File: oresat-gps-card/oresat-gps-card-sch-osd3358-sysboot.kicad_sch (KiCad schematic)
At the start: 23 parts, among them J2 Conn_01x02, J5 Conn_01x06, U1 OSD3358-512M-BSM

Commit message: Routine Push
Various small changes made
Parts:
- removed TP114, TP115, TP116, TP117, TP118, TP119, TP120, TP121, TP122, TP123, TP124, TP125, TP126: 0.03x0.04, oresat-misc:TestPoint_Pad_D1.0mm, symbol oresat-misc:Test-Point-1mm-round

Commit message: Routine Push
First attempt to clean up schematic
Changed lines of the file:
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@@
 		)
 	)
-	(global_label "GPS-EN"
+	(hierarchical_label "MAX_~{SHDN}"
 		(shape input)
-		(at 33.02 124.46 180)
-		(fields_autoplaced yes)
+		(at 33.02 99.06 180)
 		(effects
 			(font
@@
 			(justify right)
 		)
-		(property "Intersheetrefs" "${INTERSHEET_REFS}"
-			(at 22.8055 124.3806 0)
-			(show_name no)
-			(do_not_autoplace no)
-			(effects
-				(font
-					(size 1.27 1.27)
-				)
-				(justify right)
-			)
-		)
 	)
-	(global_label "STQ_UART2_TX"
+	(hierarchical_label "MAX_SPI1_CS0"
 		(shape input)
-		(at 53.34 165.1 270)
-		(fields_autoplaced yes)
+		(at 48.26 165.1 270)
 		(effects
 			(font
@@
 			(justify right)
 		)
-		(property "Intersheetrefs" "${INTERSHEET_REFS}"
-			(at 53.2606 180.9993 90)
-			(show_name no)
-			(do_not_autoplace no)
-			(effects
-				(font
-					(size 1.27 1.27)
-				)
-				(justify right)
+	)
+	(hierarchical_label "GPS-EN"
+		(shape input)
+		(at 33.02 124.46 180)
+		(effects
+			(font
+				(size 1.27 1.27)
 			)
+			(justify right)
 		)
 	)
-	(global_label "SYSBOOT2"
+	(hierarchical_label "MAX_SPI1_D0"
+		(shape input)
+		(at 43.18 165.1 270)
+		(effects
+			(font
+				(size 1.27 1.27)
+			)
+			(justify right)
+		)
+	)
+	(hierarchical_label "STQ_UART2_TX"
+		(shape input)
+		(at 53.34 165.1 270)
+		(effects
+			(font
+				(size 1.27 1.27)
+			)
+			(justify right)
+		)
+	)
+	(hierarchical_label "STQ_UART2_RX"
+		(shape input)
+		(at 50.8 165.1 270)
+		(effects
+			(font
+				(size 1.27 1.27)
+			)
+			(justify right)
+		)
+	)
+	(hierarchical_label "SYSBOOT2"
 		(shape input)
 		(at 220.98 109.22 0)
-		(fields_autoplaced yes)
 		(effects
 			(font
@@
 			(justify left)
 		)
-		(property "Intersheetrefs" "${INTERSHEET_REFS}"
-			(at 233.5015 109.22 0)
-			(show_name no)
-			(do_not_autoplace no)
-			(effects
-				(font
-					(size 1.27 1.27)
-				)
-				(justify left)
-			)
-		)
 	)
-	(global_label "STQ_UART2_RX"
+	(hierarchical_label "MAX_SPI1_SCLK"
 		(shape input)
-		(at 50.8 165.1 270)
-		(fields_autoplaced yes)
+		(at 45.72 165.1 270)
 		(effects
 			(font
@@
 			(justify right)
 		)
-		(property "Intersheetrefs" "${INTERSHEET_REFS}"
-			(at 50.7206 181.3017 90)
-			(show_name no)
-			(do_not_autoplace no)
-			(effects
-				(font
-					(size 1.27 1.27)
-				)
-				(justify right)
-			)
-		)
 	)
-	(global_label "STQ-1PPS"
+	(hierarchical_label "STQ-1PPS"
 		(shape input)
 		(at 33.02 121.92 180)
-		(fields_autoplaced yes)
 		(effects
 			(font
@@
 			(justify right)
 		)
-		(property "Intersheetrefs" "${INTERSHEET_REFS}"
-			(at 20.5679 121.8406 0)
-			(show_name no)
-			(do_not_autoplace no)
-			(effects
-				(font
-					(size 1.27 1.27)
-				)
-				(justify right)
-			)
-		)
 	)
-	(global_label "MAX_SPI1_CS0"
+	(hierarchical_label "MAX-LD"
 		(shape input)
-		(at 48.26 165.1 270)
-		(fields_autoplaced yes)
+		(at 33.02 96.52 180)
 		(effects
 			(font
@@
 			(justify right)
 		)
-		(property "Intersheetrefs" "${INTERSHEET_REFS}"
-			(at 48.1806 181.1807 90)
-			(show_name no)
-			(do_not_autoplace no)
-			(effects
-				(font
-					(size 1.27 1.27)
-				)
-				(justify right)
-			)
-		)
 	)
-	(global_label "MAX_SPI1_D0"
-		(shape input)
-		(at 43.18 165.1 270)
-		(fields_autoplaced yes)
-		(effects
-			(font
-				(size 1.27 1.27)
-			)
-			(justify right)
-		)
-		(property "Intersheetrefs" "${INTERSHEET_REFS}"
-			(at 43.1006 179.9712 90)
-			(show_name no)
-			(do_not_autoplace no)
-			(effects
-				(font
-					(size 1.27 1.27)
-				)
-				(justify right)
-			)
-		)
-	)
-	(global_label "MAX_~{SHDN}"
-		(shape input)
-		(at 33.02 99.06 180)
-		(fields_autoplaced yes)
-		(effects
-			(font
-				(size 1.27 1.27)
-			)
-			(justify right)
-		)
-		(property "Intersheetrefs" "${INTERSHEET_REFS}"
-			(at 20.7493 98.9806 0)
-			(show_name no)
-			(do_not_autoplace no)
-			(effects
-				(font
-					(size 1.27 1.27)
-				)
-				(justify right)
-			)
-		)
-	)
-	(global_label "MAX-LD"
-		(shape input)
-		(at 33.02 96.52 180)
-		(fields_autoplaced yes)
-		(effects
-			(font
-				(size 1.27 1.27)
-			)
-			(justify right)
-		)
-		(property "Intersheetrefs" "${INTERSHEET_REFS}"
-			(at 23.5917 96.4406 0)
-			(show_name no)
-			(do_not_autoplace no)
-			(effects
-				(font
-					(size 1.27 1.27)
-				)
-				(justify right)
-			)
-		)
-	)
-	(global_label "MAX_SPI1_SCLK"
-		(shape input)
-		(at 45.72 165.1 270)
-		(fields_autoplaced yes)
-		(effects
-			(font
-				(size 1.27 1.27)
-			)
-			(justify right)
-		)
-		(property "Intersheetrefs" "${INTERSHEET_REFS}"
-			(at 45.6406 182.2693 90)
-			(show_name no)
-			(do_not_autoplace no)
-			(effects
-				(font
-					(size 1.27 1.27)
-				)
-				(justify right)
-			)
-		)
-	)

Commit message: Routine Push
Schematic finished. Components laid out, chasing ERCs.
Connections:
- no-connect marks 8 -> 21
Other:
- moved on the sheet: J2, J5, R72, R73, R74, TP111, TP112, TP113, TP20, U1D

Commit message: Routine Push
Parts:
- removed TP111, TP112, TP113, TP20: 0.03x0.04, oresat-misc:TestPoint_Pad_D1.0mm, symbol oresat-misc:Test-Point-1mm-round
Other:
- note added: "All resistors are 0603 1% AEC-Q200 unless marked. All capacitors are 0603 AEC-Q200 Vw >= 16V X5R or better unless marked."

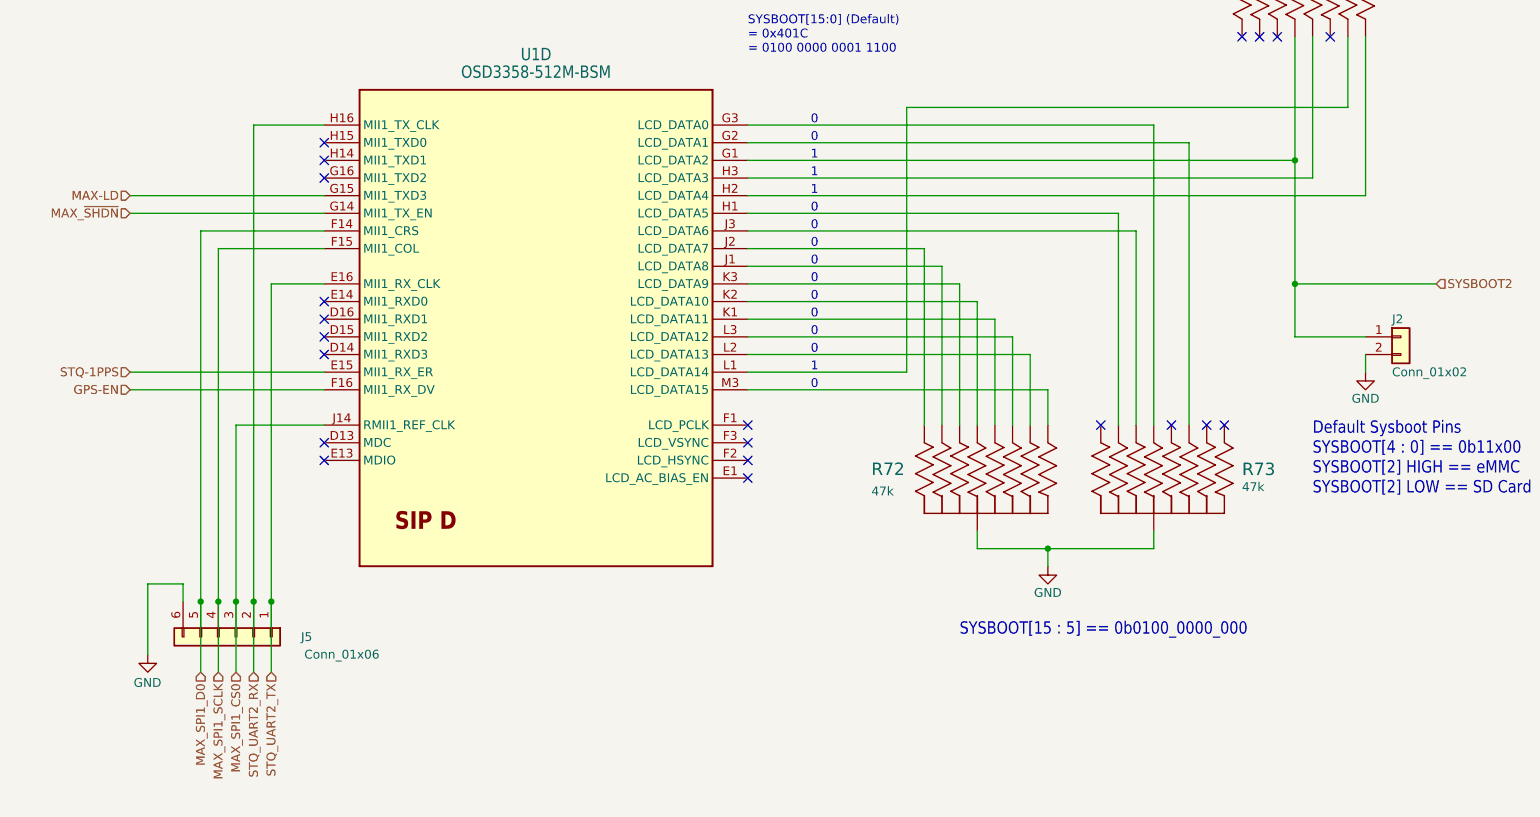
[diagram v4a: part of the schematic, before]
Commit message: General cleanup of schematic and layout
Updated .gitignore, updates DRU file, moved RF lines to RF-50-MIN (max is just too big),
lots of cleanup on the root page to make it pretty, cleaned up some redudant labels,
updated SMPM connector and added rule zone, updated PCB outline to include NPTH drills
for SMPM connectors, began cleanup of OPD.
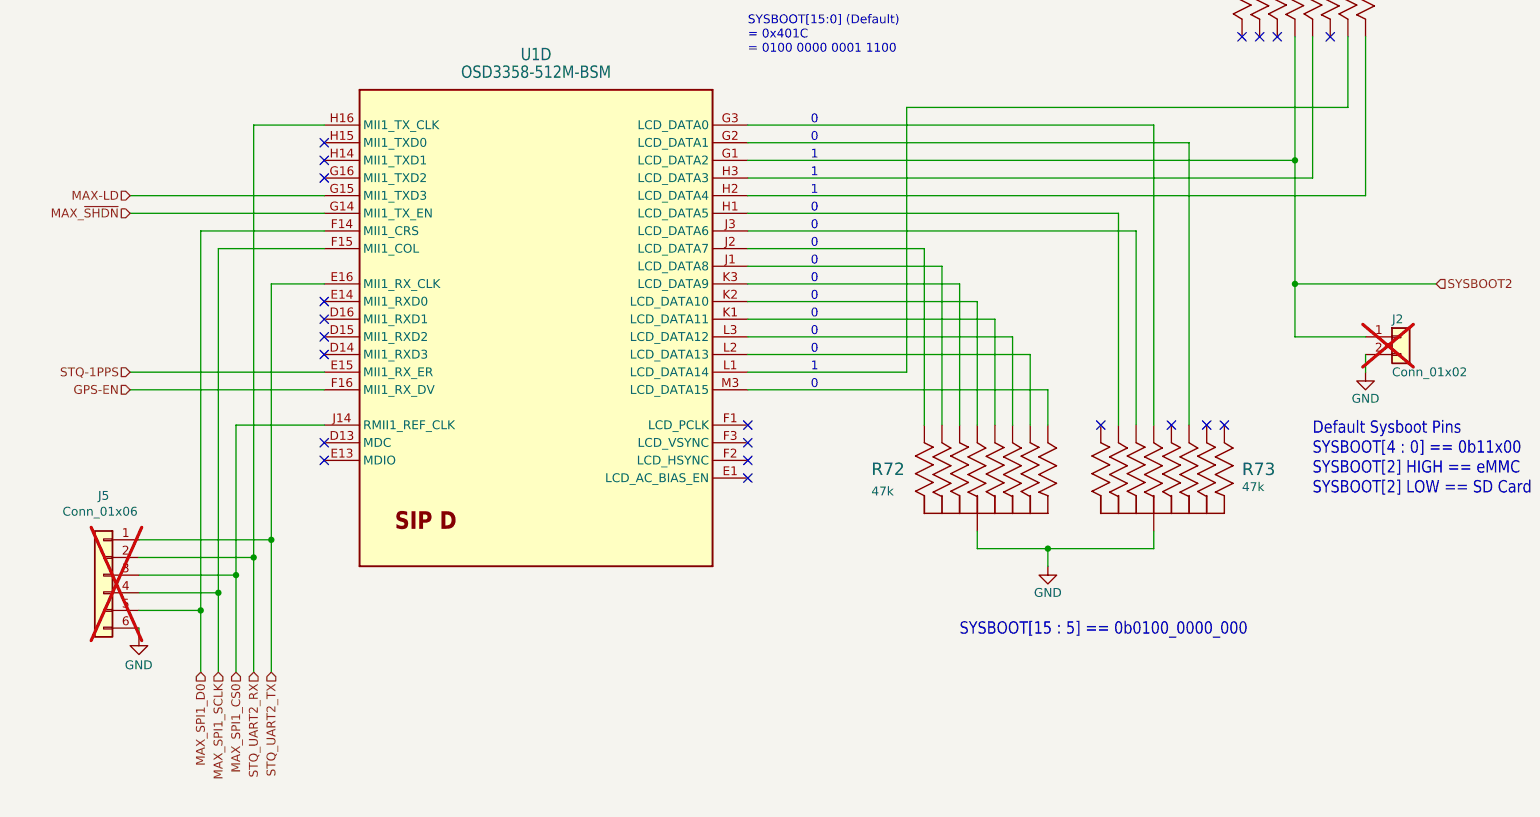
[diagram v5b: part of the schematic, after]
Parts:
- J2, J5: now not fitted
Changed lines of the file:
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@@
 	)
 	(junction
-		(at 138.43 184.15)
+		(at 140.97 180.34)
 		(diameter 0)
 		(color 0 0 0 0)
 	)
 	(junction
-		(at 146.05 184.15)
+		(at 135.89 185.42)
 		(diameter 0)
 		(color 0 0 0 0)
 	)
 	(junction
-		(at 143.51 184.15)
+		(at 143.51 177.8)
 		(diameter 0)
 		(color 0 0 0 0)
 	)
 	(junction
-		(at 135.89 184.15)
-		(diameter 0)
-		(color 0 0 0 0)
-	)
-	(junction
-		(at 140.97 184.15)
+		(at 146.05 175.26)
 		(diameter 0)
 		(color 0 0 0 0)
@@
 		(color 0 0 0 0)
 	)
+	(junction
+		(at 138.43 182.88)
+		(diameter 0)
+		(color 0 0 0 0)
+	)
 	(no_connect
 		(at 153.67 148.59)
@@
 	(wire
 		(pts
-			(xy 133.35 184.15) (xy 133.35 181.61)
+			(xy 127 187.96) (xy 127 189.23)
 		)
 		(stroke
@@
 	(wire
 		(pts
+			(xy 127 182.88) (xy 138.43 182.88)
+		)
+		(stroke
+			(width 0)
+			(type default)
+		)
+	)
+	(wire
+		(pts
 			(xy 214.63 153.67) (xy 257.81 153.67)
 		)
@@
 	(wire
 		(pts
-			(xy 135.89 184.15) (xy 135.89 130.81)
+			(xy 135.89 130.81) (xy 135.89 185.42)
 		)
 		(stroke
@@
 	(wire
 		(pts
+			(xy 127 177.8) (xy 143.51 177.8)
+		)
+		(stroke
+			(width 0)
+			(type default)
+		)
+	)
+	(wire
+		(pts
 			(xy 214.63 135.89) (xy 242.57 135.89)
 		)
@@
 	(wire
 		(pts
+			(xy 140.97 180.34) (xy 140.97 194.31)
+		)
+		(stroke
+			(width 0)
+			(type default)
+		)
+	)
+	(wire
+		(pts
 			(xy 135.89 130.81) (xy 153.67 130.81)
 		)
@@
 	(wire
 		(pts
+			(xy 138.43 182.88) (xy 138.43 194.31)
+		)
+		(stroke
+			(width 0)
+			(type default)
+		)
+	)
+	(wire
+		(pts
 			(xy 214.63 115.57) (xy 273.05 115.57)
 		)
@@
 	(wire
 		(pts
-			(xy 133.35 181.61) (xy 128.27 181.61)
-		)
-		(stroke
-			(width 0)
-			(type default)
-		)
-	)
-	(wire
-		(pts
-			(xy 138.43 184.15) (xy 138.43 194.31)
+			(xy 143.51 177.8) (xy 143.51 194.31)
 		)
 		(stroke
@@
 	(wire
 		(pts
-			(xy 138.43 133.35) (xy 138.43 184.15)
-		)
-		(stroke
-			(width 0)
-			(type default)
-		)
-	)
-	(wire
-		(pts
 			(xy 247.65 176.53) (xy 257.81 176.53)
 		)
@@
 	(wire
 		(pts
-			(xy 146.05 138.43) (xy 146.05 184.15)
+			(xy 127 180.34) (xy 140.97 180.34)
 		)
 		(stroke
@@
 	(wire
 		(pts
+			(xy 127 185.42) (xy 135.89 185.42)
+		)
+		(stroke
+			(width 0)
+			(type default)
+		)
+	)
+	(wire
+		(pts
 			(xy 245.11 138.43) (xy 245.11 158.75)
 		)
@@
 	(wire
 		(pts
+			(xy 127 175.26) (xy 146.05 175.26)
+		)
+		(stroke
+			(width 0)
+			(type default)
+		)
+	)
+	(wire
+		(pts
 			(xy 240.03 133.35) (xy 240.03 158.75)
 		)
@@
 	(wire
 		(pts
-			(xy 128.27 181.61) (xy 128.27 191.77)
-		)
-		(stroke
-			(width 0)
-			(type default)
-		)
-	)
-	(wire
-		(pts
 			(xy 293.37 138.43) (xy 293.37 146.05)
 		)
@@
 	(wire
 		(pts
-			(xy 135.89 184.15) (xy 135.89 194.31)
+			(xy 135.89 185.42) (xy 135.89 194.31)
+		)
+		(stroke
+			(width 0)
+			(type default)
+		)
+	)
+	(wire
+		(pts
+			(xy 140.97 158.75) (xy 140.97 180.34)
 		)
 		(stroke
@@
 		)
 	)
-	(wire
-		(pts
-			(xy 143.51 115.57) (xy 143.51 184.15)
-		)
-		(stroke
-			(width 0)
-			(type default)
-		)
-	)
 	(polyline
 		(pts
@@
 	(wire
 		(pts
+			(xy 146.05 175.26) (xy 146.05 194.31)
+		)
+		(stroke
+			(width 0)
+			(type default)
+		)
+	)
+	(wire
+		(pts
 			(xy 214.63 148.59) (xy 255.27 148.59)
 		)
@@
 	(wire
 		(pts
-			(xy 140.97 184.15) (xy 140.97 158.75)
-		)
-		(stroke
-			(width 0)
-			(type default)
-		)
-	)
-	(wire
-		(pts
 			(xy 125.73 128.27) (xy 153.67 128.27)
 		)
@@
 	(wire
 		(pts
-			(xy 140.97 184.15) (xy 140.97 194.31)
-		)
-		(stroke
-			(width 0)
-			(type default)
-		)
-	)
-	(wire
-		(pts
 			(xy 214.63 138.43) (xy 245.11 138.43)
 		)
@@
 	(wire
 		(pts
+			(xy 143.51 115.57) (xy 143.51 177.8)
+		)
+		(stroke
+			(width 0)
+			(type default)
+		)
+	)
+	(wire
+		(pts
 			(xy 293.37 138.43) (xy 313.69 138.43)
 		)
@@
 	(wire
 		(pts
-			(xy 143.51 184.15) (xy 143.51 194.31)
-		)
-		(stroke
-			(width 0)
-			(type default)
-		)
-	)
-	(wire
-		(pts
-			(xy 146.05 184.15) (xy 146.05 194.31)
+			(xy 146.05 138.43) (xy 146.05 175.26)
 		)
 		(stroke
@@
 		(pts
 			(xy 295.91 85.09) (xy 295.91 87.63)
+		)
+		(stroke
+			(width 0)
+			(type default)
+		)
+	)
+	(wire
+		(pts
+			(xy 138.43 133.35) (xy 138.43 182.88)
 		)
 		(stroke
@@
 		(on_board yes)
 		(in_pos_files yes)
-		(dnp no)
+		(dnp yes)
 		(property "Reference" "J2"
 			(at 307.34 143.51 0)
@@
 	(symbol
 		(lib_id "Connector_Generic:Conn_01x06")
-		(at 140.97 189.23 270)
+		(at 121.92 180.34 0)
+		(mirror y)
 		(unit 1)
 		(body_style 1)
@@
 		(on_board yes)
 		(in_pos_files yes)
-		(dnp no)
+		(dnp yes)
 		(property "Reference" "J5"
-			(at 151.13 189.23 90)
+			(at 121.92 168.91 0)
 			(show_name no)
 			(do_not_autoplace no)
@@
 		)
 		(property "Value" "Conn_01x06"
-			(at 156.21 191.77 90)
+			(at 121.412 171.196 0)
 			(show_name no)
 			(do_not_autoplace no)
@@
 		)
 		(property "Footprint" "Connector_PinHeader_2.54mm:PinHeader_1x06_P2.54mm_Vertical"
-			(at 140.97 189.23 0)
+			(at 121.92 180.34 0)
 			(hide yes)
 			(show_name no)
@@
 		)
 		(property "Datasheet" ""
-			(at 140.97 189.23 0)
+			(at 121.92 180.34 0)
 			(hide yes)
 			(show_name no)
@@
 		)
 		(property "Description" "Generic connector, single row, 01x06, script generated (kicad-library-utils/schlib/autogen/connector/)"
-			(at 140.97 189.23 0)
+			(at 121.92 180.34 0)
 			(hide yes)
 			(show_name no)
@@
 	(symbol
 		(lib_id "power:GND")
-		(at 128.27 191.77 0)
+		(at 127 189.23 0)
 		(unit 1)
 		(body_style 1)
@@
 		(dnp no)
 		(property "Reference" "#GND0151"
-			(at 128.27 198.12 0)
+			(at 127 195.58 0)
 			(hide yes)
 			(show_name no)
@@
 		)
 		(property "Value" "GND"
-			(at 126.238 195.834 0)
+			(at 124.968 193.294 0)
 			(show_name no)
 			(do_not_autoplace no)
@@
 		)
 		(property "Footprint" ""
-			(at 128.27 191.77 0)
+			(at 127 189.23 0)
 			(hide yes)
 			(show_name no)
@@
 		)
 		(property "Datasheet" ""
-			(at 128.27 191.77 0)
+			(at 127 189.23 0)
 			(hide yes)
 			(show_name no)
@@
 		)
 		(property "Description" "Power symbol creates a global label with name \"GND\" , ground"
-			(at 128.27 191.77 0)
-			(hide yes)
-			(show_name no)
+			(at 127 189.23 0)
+			(hide yes)
+			(show_name no)
